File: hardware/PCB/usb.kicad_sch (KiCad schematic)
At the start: 5 parts, among them J8 USB_C_Receptacle_USB2.0_16P, U8 SRV05-4

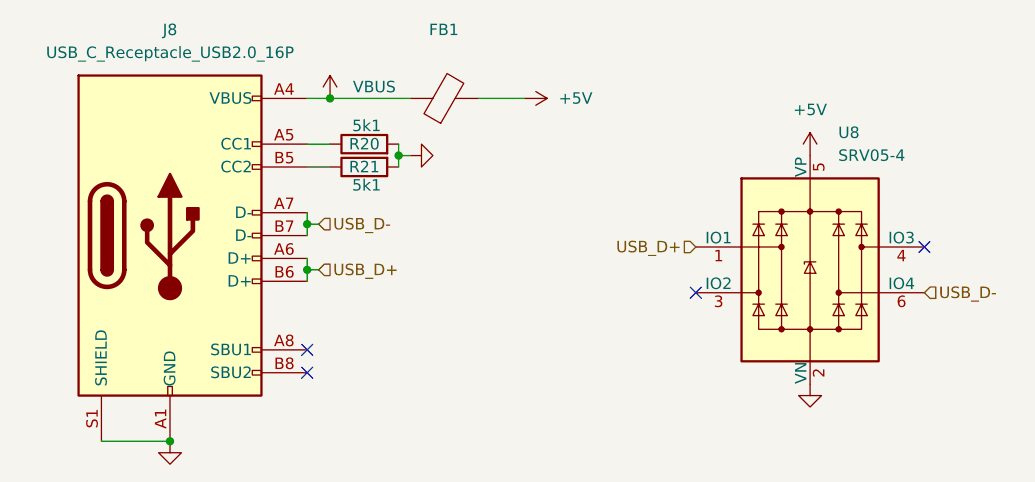
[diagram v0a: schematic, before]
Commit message: Finished schematic for LoRa, added BME280
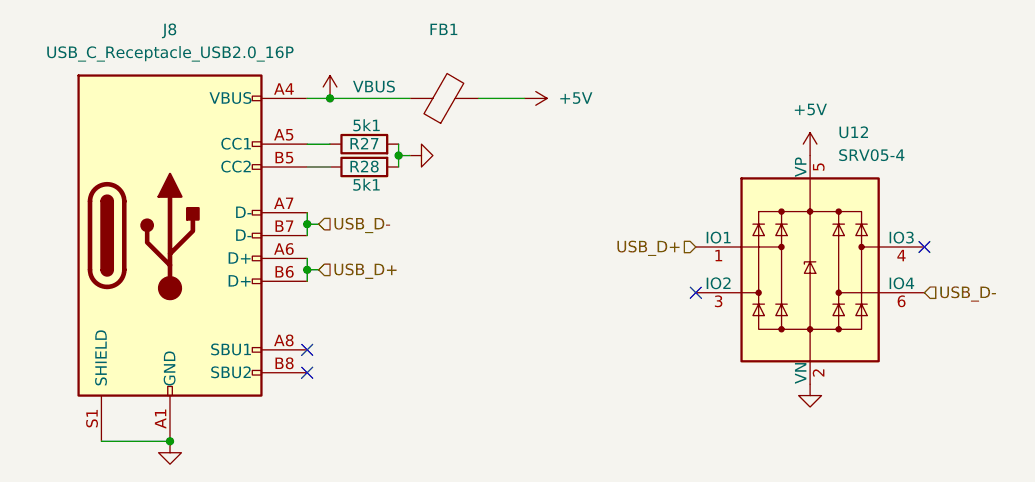
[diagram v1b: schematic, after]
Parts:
- renumbered R20 to R27, R21 to R28, U8 to U12
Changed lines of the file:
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@@
 		(dnp no)
 		(fields_autoplaced yes)
-		(property "Reference" "U8"
+		(property "Reference" "U12"
 			(at 170.7581 87.63 0)
 			(effects
@@
 			(project "Startracker"
 				(path "/45ea479c-a8ef-4c14-88b0-391ede4fd156/a9fb2034-2b0b-4250-a30a-658fa52241d9"
-					(reference "U8")
+					(reference "U12")
 					(unit 1)
 				)
@@
 		(dnp no)
 		(fields_autoplaced yes)
-		(property "Reference" "#PWR074"
+		(property "Reference" "#PWR0109"
 			(at 129.54 90.17 0)
 			(effects
@@
 			(project "Startracker"
 				(path "/45ea479c-a8ef-4c14-88b0-391ede4fd156/a9fb2034-2b0b-4250-a30a-658fa52241d9"
-					(reference "#PWR074")
+					(reference "#PWR0109")
 					(unit 1)
 				)
@@
 		(dnp no)
 		(fields_autoplaced yes)
-		(property "Reference" "#PWR077"
+		(property "Reference" "#PWR0112"
 			(at 96.52 128.27 0)
 			(effects
@@
 			(project "Startracker"
 				(path "/45ea479c-a8ef-4c14-88b0-391ede4fd156/a9fb2034-2b0b-4250-a30a-658fa52241d9"
-					(reference "#PWR077")
+					(reference "#PWR0112")
 					(unit 1)
 				)
@@
 		(dnp no)
 		(fields_autoplaced yes)
-		(property "Reference" "#PWR075"
+		(property "Reference" "#PWR0110"
 			(at 167.64 93.98 0)
 			(effects
@@
 			(project "Startracker"
 				(path "/45ea479c-a8ef-4c14-88b0-391ede4fd156/a9fb2034-2b0b-4250-a30a-658fa52241d9"
-					(reference "#PWR075")
+					(reference "#PWR0110")
 					(unit 1)
 				)
@@
 		(dnp no)
 		(fields_autoplaced yes)
-		(property "Reference" "#PWR072"
+		(property "Reference" "#PWR0107"
 			(at 114.3 87.63 0)
 			(effects
@@
 			(project "Startracker"
 				(path "/45ea479c-a8ef-4c14-88b0-391ede4fd156/a9fb2034-2b0b-4250-a30a-658fa52241d9"
-					(reference "#PWR072")
+					(reference "#PWR0107")
 					(unit 1)
 				)
@@
 		(on_board yes)
 		(dnp no)
-		(property "Reference" "R20"
+		(property "Reference" "R27"
 			(at 118.11 88.9 90)
 			(effects
@@
 			(project "Startracker"
 				(path "/45ea479c-a8ef-4c14-88b0-391ede4fd156/a9fb2034-2b0b-4250-a30a-658fa52241d9"
-					(reference "R20")
+					(reference "R27")
 					(unit 1)
 				)
@@
 		(on_board yes)
 		(dnp no)
-		(property "Reference" "R21"
+		(property "Reference" "R28"
 			(at 118.11 91.44 90)
 			(effects
@@
 			(project "Startracker"
 				(path "/45ea479c-a8ef-4c14-88b0-391ede4fd156/a9fb2034-2b0b-4250-a30a-658fa52241d9"
-					(reference "R21")
+					(reference "R28")
 					(unit 1)
 				)
@@
 		(dnp no)
 		(fields_autoplaced yes)
-		(property "Reference" "#PWR076"
+		(property "Reference" "#PWR0111"
 			(at 167.64 121.92 0)
 			(effects
@@
 			(project "Startracker"
 				(path "/45ea479c-a8ef-4c14-88b0-391ede4fd156/a9fb2034-2b0b-4250-a30a-658fa52241d9"
-					(reference "#PWR076")
+					(reference "#PWR0111")
 					(unit 1)
 				)
@@
 		(dnp no)
 		(fields_autoplaced yes)
-		(property "Reference" "#PWR073"
+		(property "Reference" "#PWR0108"
 			(at 132.08 83.82 0)
 			(effects
@@
 			(project "Startracker"
 				(path "/45ea479c-a8ef-4c14-88b0-391ede4fd156/a9fb2034-2b0b-4250-a30a-658fa52241d9"
-					(reference "#PWR073")
-					(unit 1)
-				)
+					(reference "#PWR0108")
+					(unit 1)
+				)
